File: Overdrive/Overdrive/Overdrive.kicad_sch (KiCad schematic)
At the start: 35 parts, among them J1 Conn_02x08_Counter_Clockwise, Q1 2N3904, Q2 2N3904, U1 RTB05W, U2 AD5160, U3 TL071, U4 TL071, U5 AD8400ARZ1

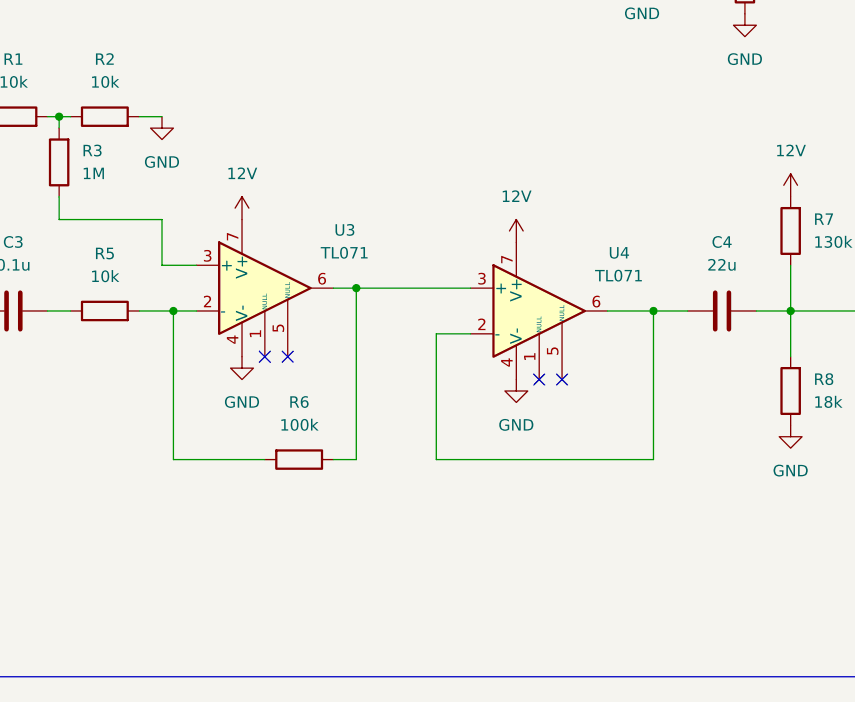
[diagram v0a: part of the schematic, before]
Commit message: finished schematic for phase 90 and implemented the correct op-amps for overdrive
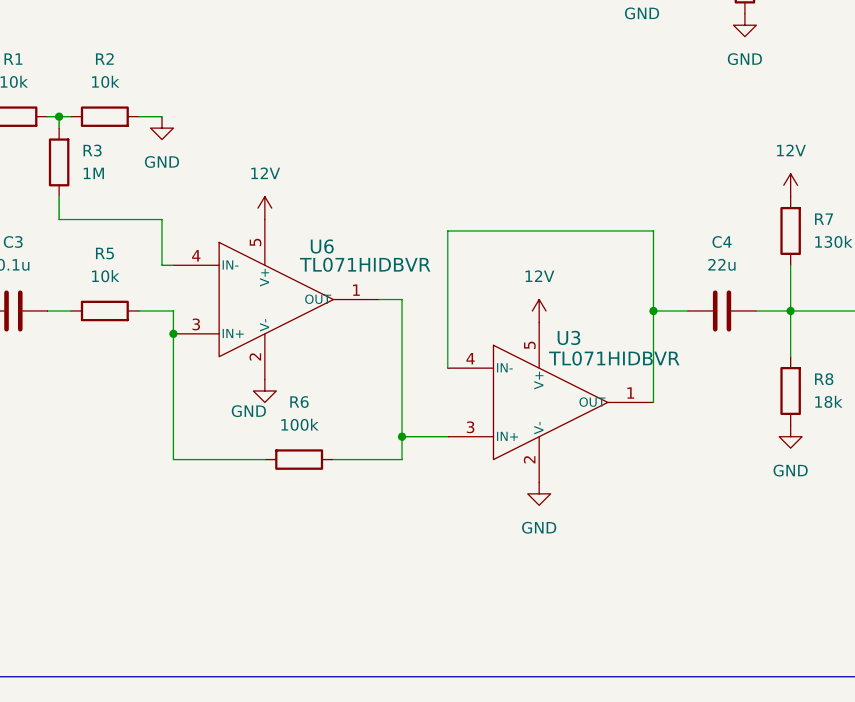
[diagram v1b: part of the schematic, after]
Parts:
- removed U3, U4: TL071, symbol Amplifier_Operational:TL071
- added U3, U6: TL071HIDBVR, SOT23_DBV_5_TEX, symbol TL071HIDBVR:TL071HIDBVR
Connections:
- net 12V: now also U3.5 (V+), U6.5 (V+)
- net GND: now also U3.2 (V-), U6.2 (V-)
- net at R5.2, R6.2: now also U6.3 (IN+)
- net at C4.1: now also U3.1 (OUT), U3.4 (IN-)
- net at R6.1: now also U3.3 (IN+), U6.1 (OUT)
- net at R3.1: now also U6.4 (IN-)
- no-connect marks 8 -> 4

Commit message: changed out potentiometer for one that can do higher analog voltages
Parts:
- U3, U6: footprint SOT23_DBV_5_TEX -> TL071:TL071HIDBVR
- U5: footprint R_8_ADI -> footprints:R_8_ADI
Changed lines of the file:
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@@
 			)
 		)
-		(property "Footprint" "R_8_ADI"
+		(property "Footprint" "footprints:R_8_ADI"
 			(at 241.808 98.806 0)
 			(effects
@@
 			)
 		)
-		(property "Footprint" "SOT23_DBV_5_TEX"
+		(property "Footprint" "TL071:TL071HIDBVR"
 			(at 91.44 95.25 0)
 			(effects
@@
 			)
 		)
-		(property "Footprint" "SOT23_DBV_5_TEX"
+		(property "Footprint" "TL071:TL071HIDBVR"
 			(at 121.92 106.68 0)
 			(effects

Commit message: finished overdrive layout
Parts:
- removed D1, D2, D3, D4, D5: 1N4148, Diode_THT:D_DO-35_SOD27_P7.62mm_Horizontal, symbol Diode:1N4148
- removed J1: Conn_02x08_Counter_Clockwise, Connector_PinHeader_1.00mm:PinHeader_2x08_P1.00mm_Horizontal, symbol Connector_Generic:Conn_02x08_Counter_Clockwise
- removed U1: RTB05W, Converter_DCDC:Converter_DCDC_RECOM_R-78B-2.0_THT, symbol Regulator_Switching:R-78B1.5-2.0
- added D1, D2, D3, D4, D5: 1N4148W, Diode_SMD:D_SOD-123, symbol Diode:1N4148W
- added J1: Conn_02x08_Odd_Even, Connector_PinHeader_2.54mm:PinHeader_2x08_P2.54mm_Horizontal, symbol Connector_Generic:Conn_02x08_Odd_Even
- added U4: ADP7118AUJZ-4.5-R7, ADP7118AUJZ-4-5-R7:UJ-5_ADI, symbol ADP7118AUJZ-4-5-R7:ADP7118AUJZ-4.5-R7
- C1, C2: value 4.7u -> 2.2u; footprint Capacitor_SMD:C_0603_1608Metric_Pad1.08x0.95mm_HandSolder -> Capacitor_SMD:C_0603_1608Metric
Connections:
- net 12V: now also J1.1 (Pin_1), J1.2 (Pin_2), U4.1 (VIN), U4.3 (EN); no longer U5.6 (VDD)
- net CS0: now also J1.11 (Pin_11)
- net CS1: now also J1.7 (Pin_7)
- net GND: now also C8.1, D5.2 (A), J1.13 (Pin_13), J1.14 (Pin_14), J1.3 (Pin_3), J1.4 (Pin_4), U4.2 (GND)
- net GUITAR_IN: now also J1.8 (Pin_8)
- net GUITAR_OUT: now also J1.10 (Pin_10)
- net MOSI: now also J1.12 (Pin_12)
- net SPI_CLK: now also J1.6 (Pin_6)
- net at C7.2, C8.2, R14.2: now also D1.1 (K)
- net 3.3V renamed 5V
- net 5V: now also U5.6 (VDD), U4.4 (SENSE), U4.5 (VOUT)
- new net: D4.2 (A), D5.1 (K)
- new net: D2.2 (A), D3.1 (K)
- new net: D3.2 (A), D4.1 (K)
- new net: D1.2 (A), D2.1 (K)

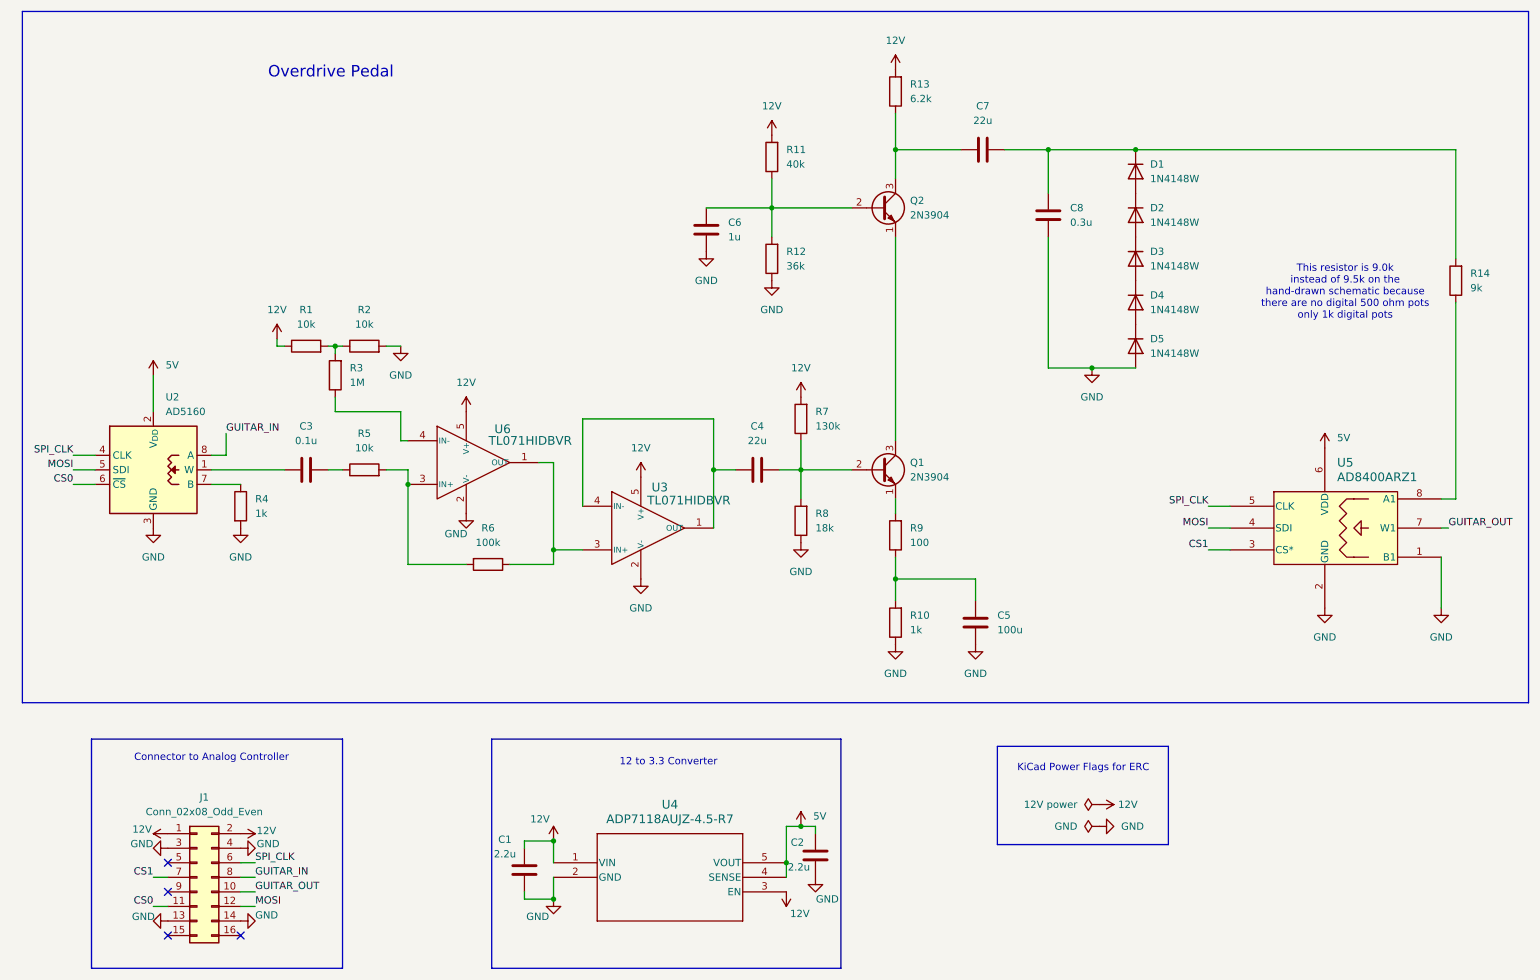
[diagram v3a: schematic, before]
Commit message: overdrive updates to conform with new connector
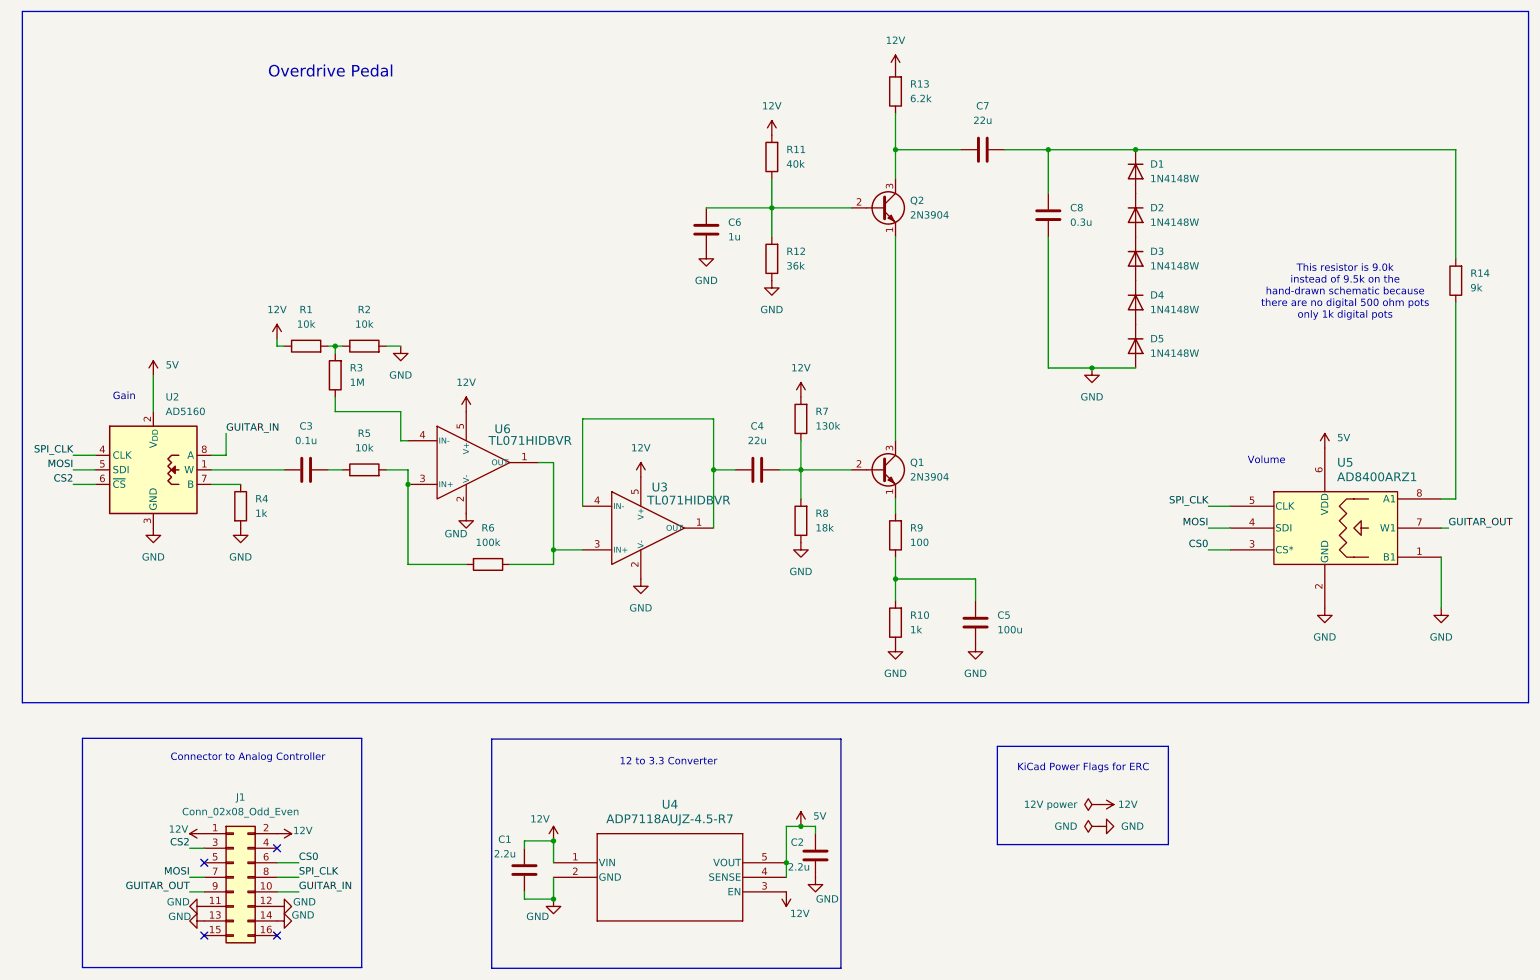
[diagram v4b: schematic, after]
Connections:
- net CS0: now also J1.6 (Pin_6), U5.3 (CS*); no longer J1.11 (Pin_11), U2.6 (~{CS})
- net GND: now also J1.11 (Pin_11), J1.12 (Pin_12); no longer J1.3 (Pin_3), J1.4 (Pin_4)
- net GUITAR_IN: now also J1.10 (Pin_10); no longer J1.8 (Pin_8)
- net GUITAR_OUT: now also J1.9 (Pin_9); no longer J1.10 (Pin_10)
- net MOSI: now also J1.7 (Pin_7); no longer J1.12 (Pin_12)
- net SPI_CLK: now also J1.8 (Pin_8); no longer J1.6 (Pin_6)
- removed net CS1: J1.7 (Pin_7), U5.3 (CS*)
- new net CS2: J1.3 (Pin_3), U2.6 (~{CS})
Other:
- note added: "Gain"
- note added: "Volume"

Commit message: added buffers and caps for op-amps on effect boards
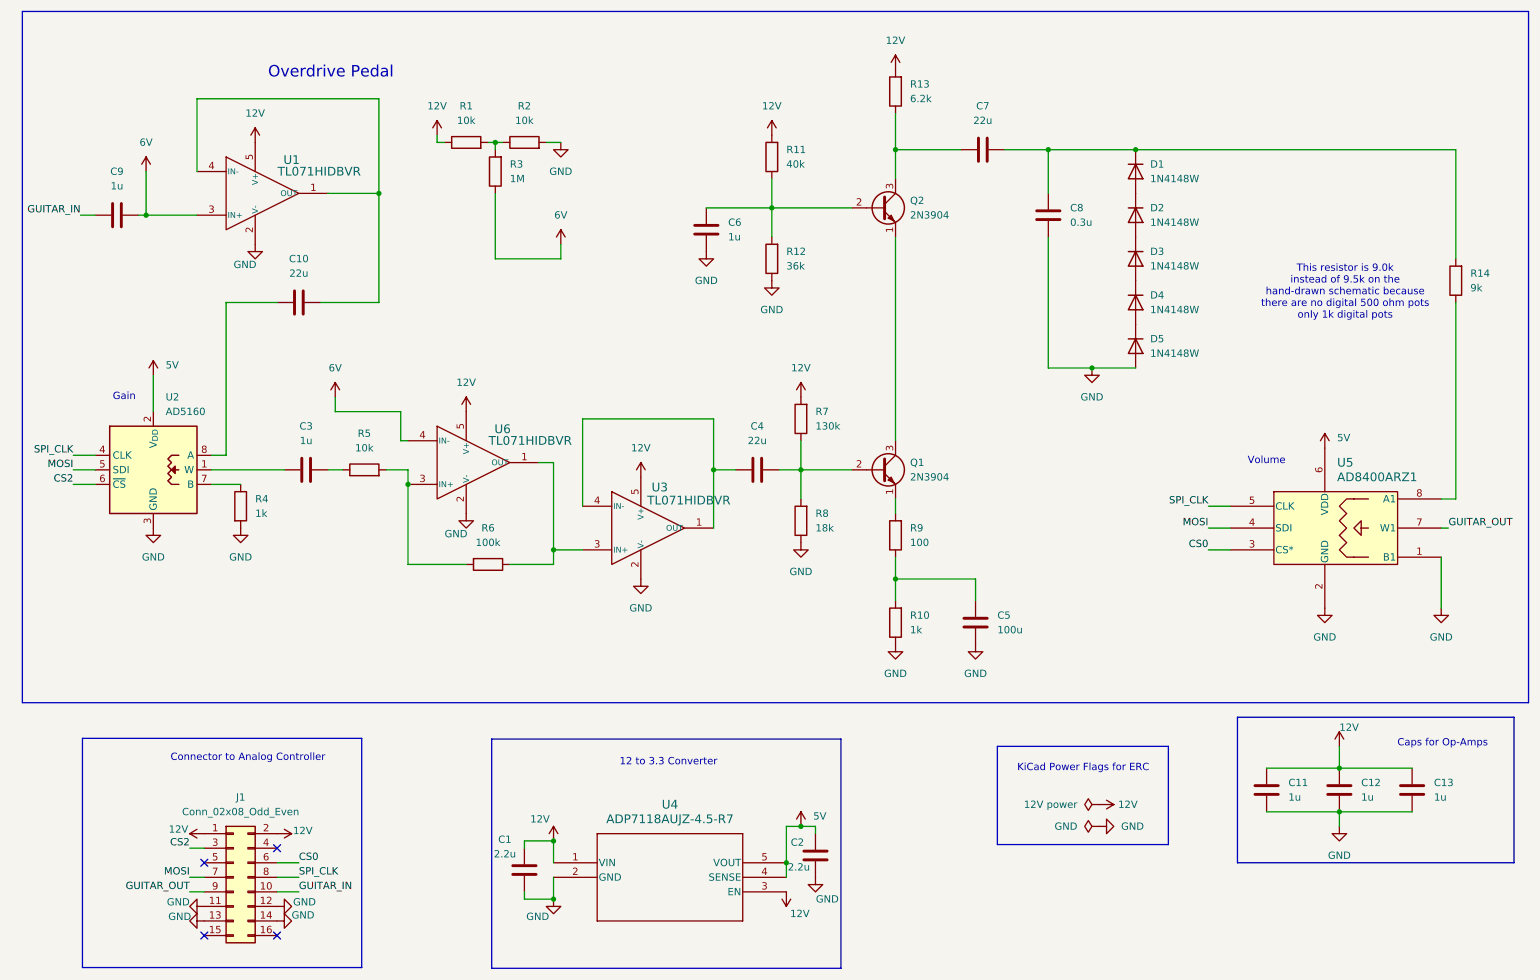
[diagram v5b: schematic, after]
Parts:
- added C10: 22u, Capacitor_SMD:C_0603_1608Metric, symbol Device:C
- added C11, C12, C13, C9: 1u, Capacitor_SMD:C_0603_1608Metric, symbol Device:C
- added U1: TL071HIDBVR, TL071:TL071HIDBVR, symbol TL071HIDBVR:TL071HIDBVR
- C3: value 0.1u -> 1u
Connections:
- net 12V: now also C11.2, C12.2, C13.2, U1.5 (V+)
- net GND: now also C11.1, C12.1, C13.1, U1.2 (V-)
- net GUITAR_IN: now also C9.1; no longer U2.8 (A)
- net 6V: now reaches R3.1, U6.4 (IN-)
- net 6V: now also C9.2, U1.3 (IN+)
- new net: C10.1, U2.8 (A)
- new net: C10.2, U1.1 (OUT), U1.4 (IN-)
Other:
- note added: "Caps for Op-Amps"
- moved on the sheet: R1, R2, R3

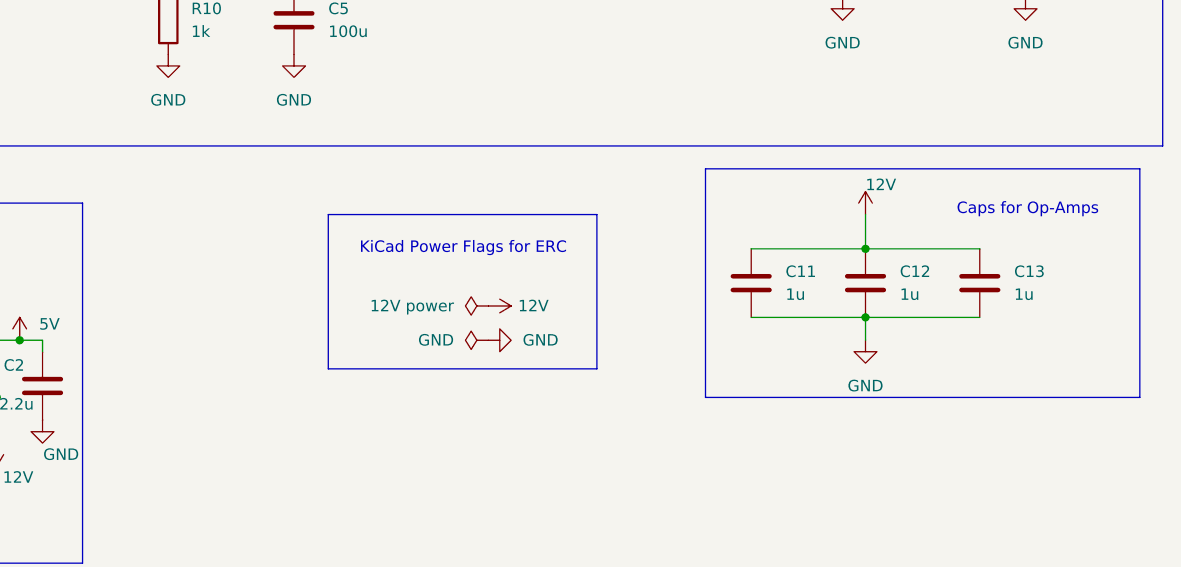
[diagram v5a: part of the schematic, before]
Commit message: board fixes for Overdrive based off of Joseph's reviews
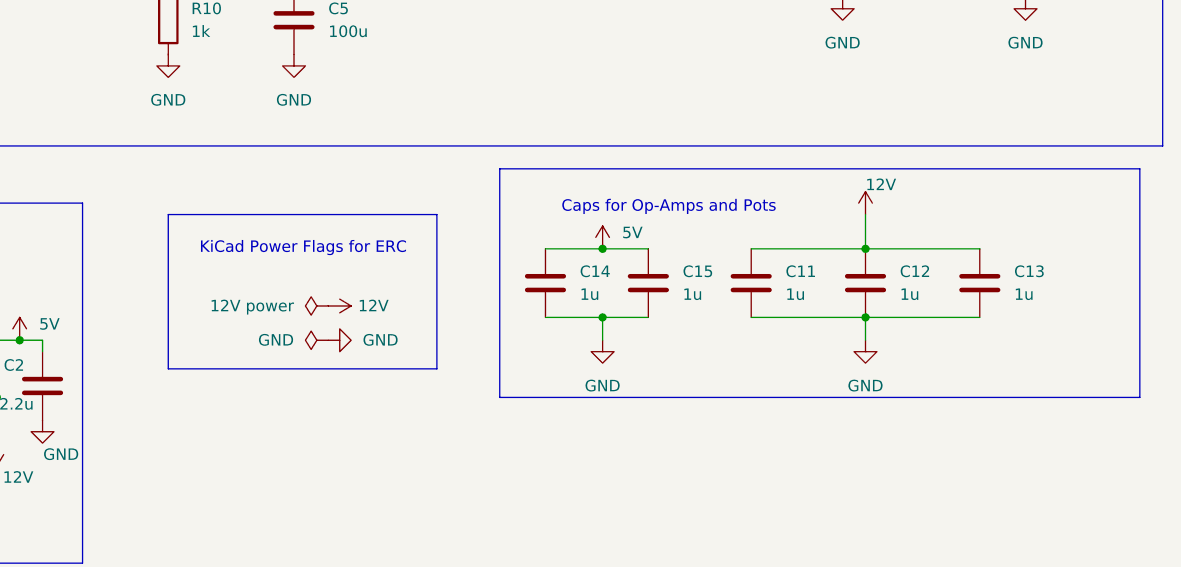
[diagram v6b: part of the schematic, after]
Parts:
- added C14, C15: 1u, Capacitor_SMD:C_0603_1608Metric, symbol Device:C
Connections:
- net 5V: now also C14.2, C15.2
- net GND: now also C14.1, C15.1
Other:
- note added: "Caps for Op-Amps and Pots"
- note removed: "Caps for Op-Amps"
